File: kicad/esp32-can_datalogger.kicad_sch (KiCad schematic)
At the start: 60 parts, among them J1 USB_C_Receptacle_USB2.0_16P, J2 USB_C_Receptacle_USB2.0_16P, J3 USB_C_Receptacle_USB2.0_16P, J4 USB_C_Receptacle_USB2.0_16P, J5 USB_C_Receptacle_USB2.0_16P, J6 USB_C_Receptacle_USB2.0_16P, J7 Conn_Coaxial, J8 MicroSD, J9 Conn_01x04_Socket, SW1 SW_Push, SW2 SW_Push, SW3 SW_Push, SW4 SW_Push, U2 PA1616D, U3 PI4ULS3V204LEX, U4 AZ1117-1.8, U5 TJA1051T, U6 TJA1051T, U7 ICM-20948

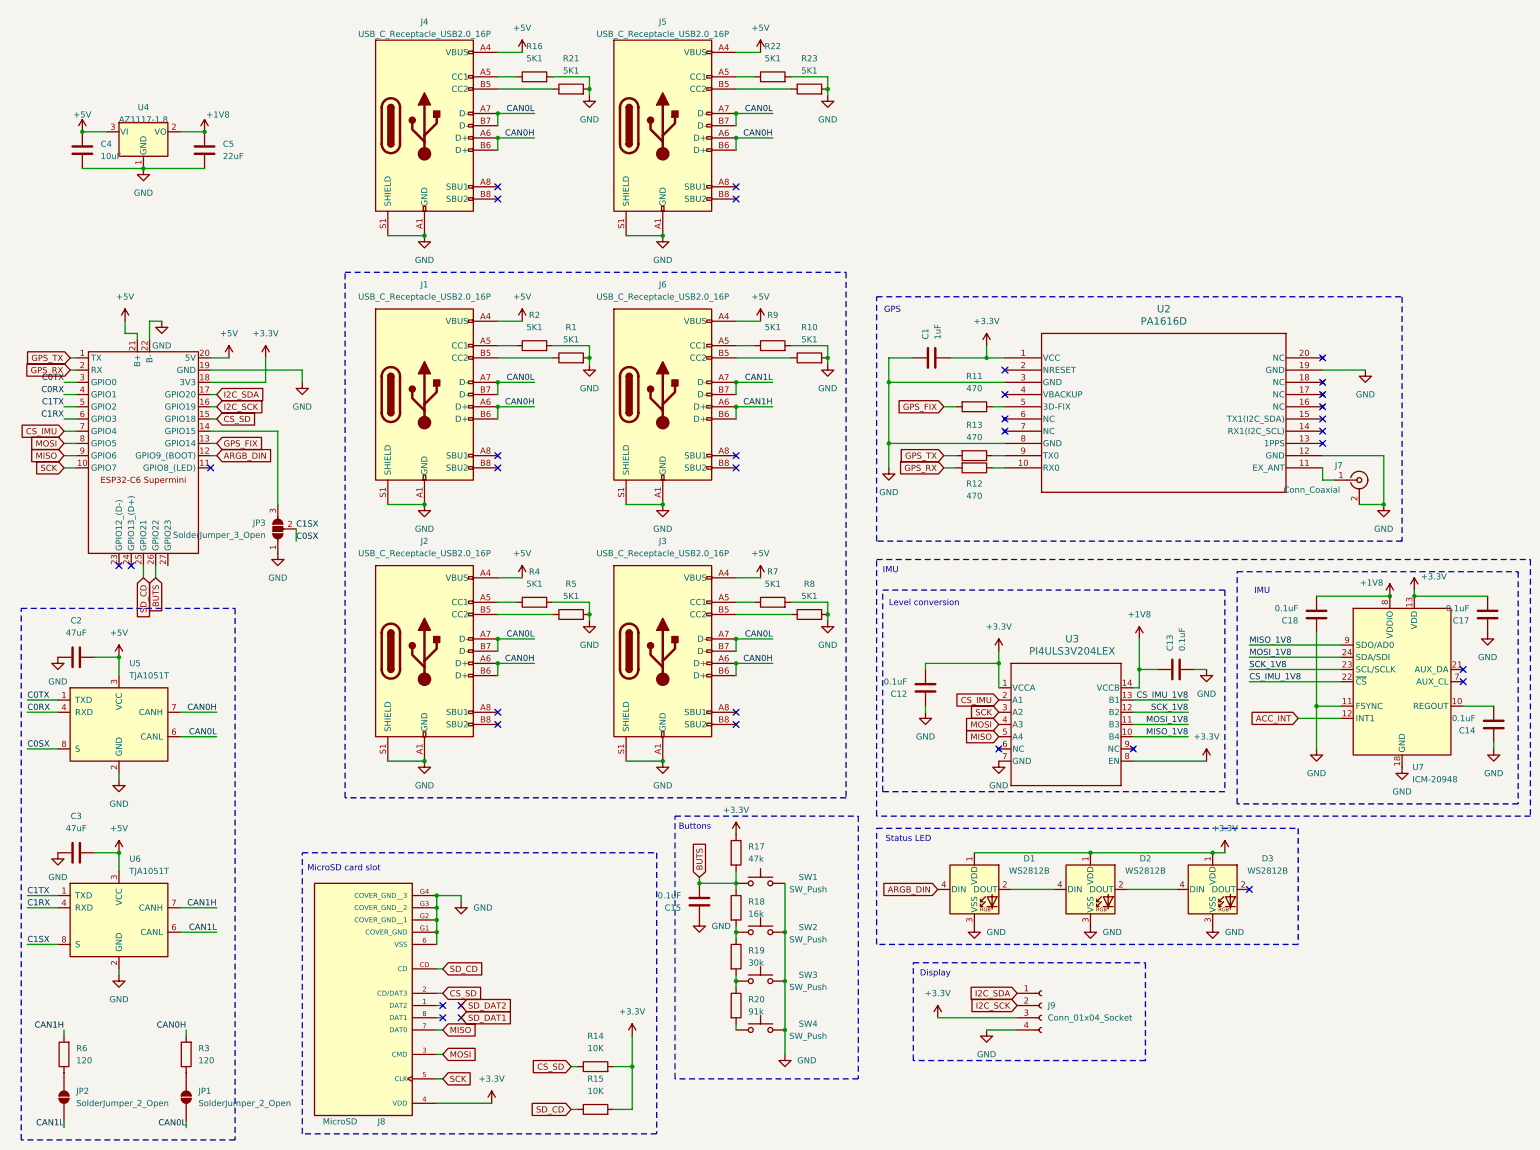
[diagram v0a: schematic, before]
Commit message: switch RX-TX for GPS
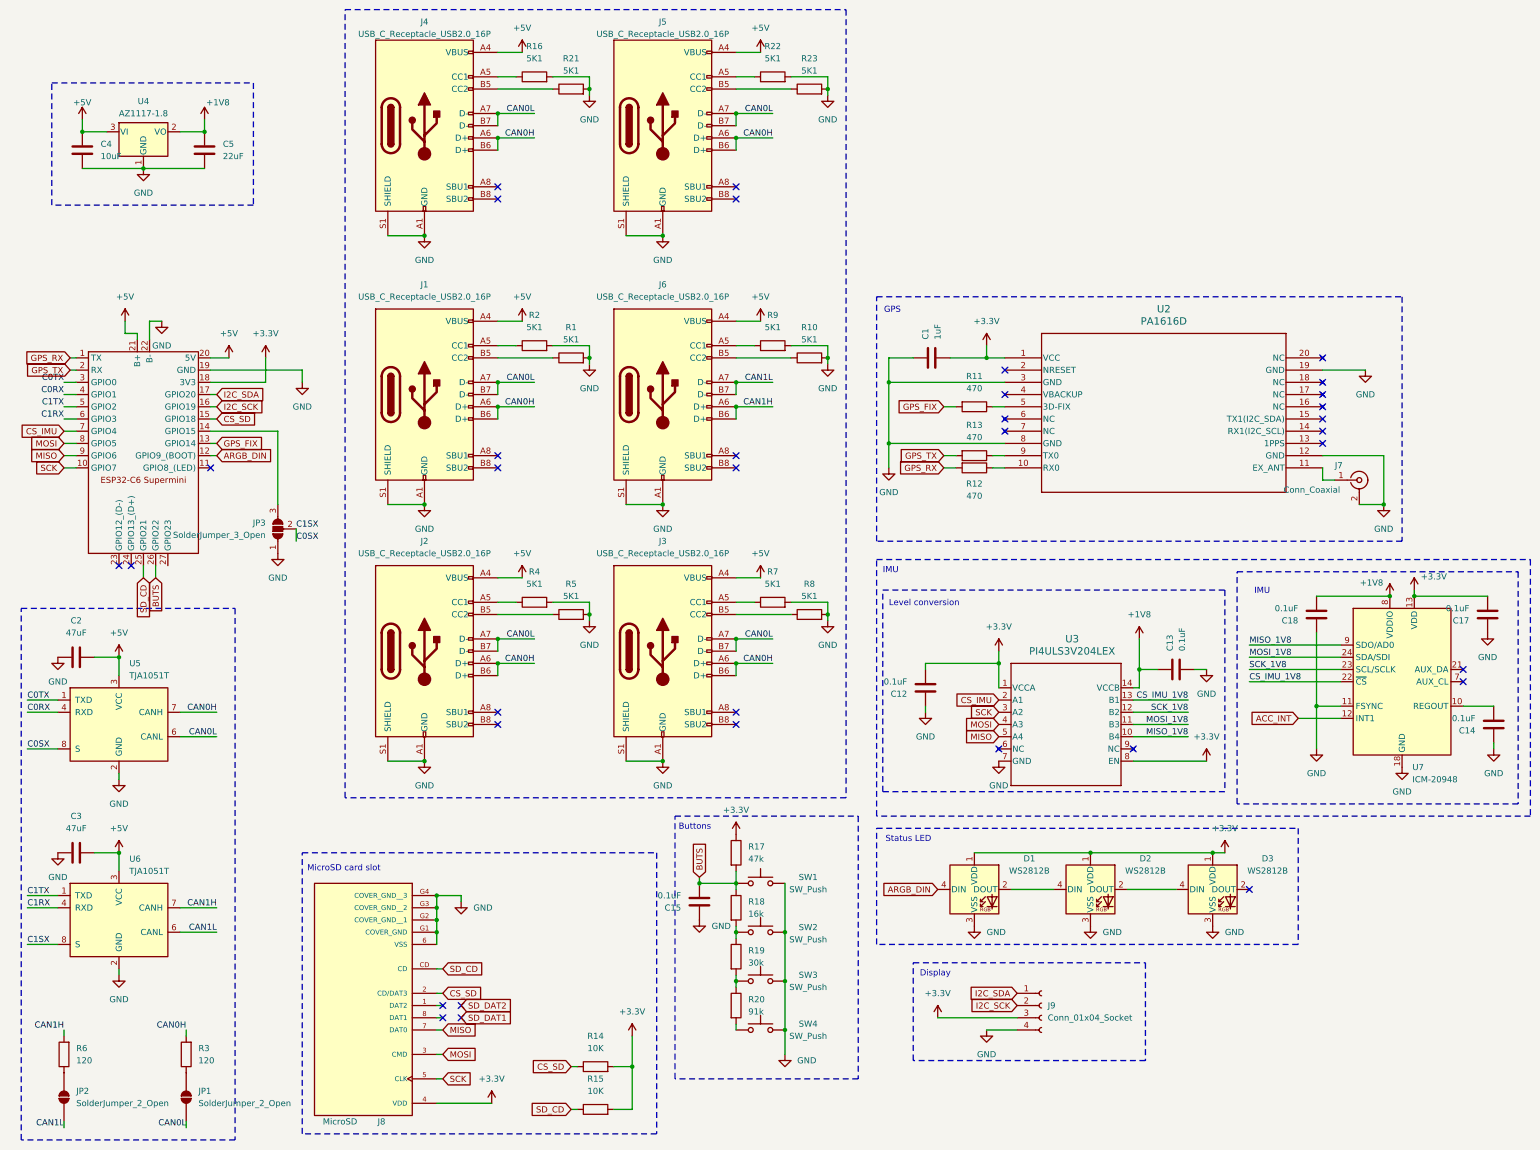
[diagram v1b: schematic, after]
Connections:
- net GPS_RX: now also U1.1 (TX); no longer U1.2 (RX)
- net GPS_TX: now also U1.2 (RX); no longer U1.1 (TX)
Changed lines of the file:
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@@
 	)
 	(rectangle
-		(start 81.28 12.7)
+		(start 20.32 -26.67)
+		(end 62.23 -1.27)
+		(stroke
+			(width 0)
+			(type dash)
+		)
+		(fill
+			(type none)
+		)
+	)
+	(rectangle
+		(start 81.28 -41.91)
 		(end 185.42 121.92)
 		(stroke
@@
 	)
 	(junction
+		(at 26.67 -16.51)
+		(diameter 0)
+		(color 0 0 0 0)
+	)
+	(junction
 		(at 147.32 114.3)
 		(diameter 0)
@@
 	)
 	(junction
-		(at 26.67 -16.51)
-		(diameter 0)
-		(color 0 0 0 0)
-	)
-	(junction
 		(at 97.79 60.96)
 		(diameter 0)
@@
 	(wire
 		(pts
+			(xy 52.07 -19.05) (xy 52.07 -16.51)
+		)
+		(stroke
+			(width 0)
+			(type default)
+		)
+	)
+	(wire
+		(pts
 			(xy 113.03 40.64) (xy 120.65 40.64)
 		)
@@
 	(wire
 		(pts
+			(xy 26.67 -19.05) (xy 26.67 -16.51)
+		)
+		(stroke
+			(width 0)
+			(type default)
+		)
+	)
+	(wire
+		(pts
 			(xy 34.29 92.71) (xy 34.29 96.52)
 		)
@@
 		)
 	)
+	(global_label "GPS_TX"
+		(shape input)
+		(at 24.13 33.02 180)
+		(fields_autoplaced yes)
+		(effects
+			(font
+				(size 1.27 1.27)
+			)
+			(justify right)
+		)
+		(property "Intersheetrefs" "${INTERSHEET_REFS}"
+			(at 14.2506 33.02 0)
+			(hide yes)
+			(show_name no)
+			(do_not_autoplace no)
+			(effects
+				(font
+					(size 1.27 1.27)
+				)
+				(justify right)
+			)
+		)
+	)
 	(global_label "CS_SD"
 		(shape input)
@@
 		)
 	)
+	(global_label "GPS_RX"
+		(shape input)
+		(at 24.13 30.48 180)
+		(fields_autoplaced yes)
+		(effects
+			(font
+				(size 1.27 1.27)
+			)
+			(justify right)
+		)
+		(property "Intersheetrefs" "${INTERSHEET_REFS}"
+			(at 13.9482 30.48 0)
+			(hide yes)
+			(show_name no)
+			(do_not_autoplace no)
+			(effects
+				(font
+					(size 1.27 1.27)
+				)
+				(justify right)
+			)
+		)
+	)
 	(global_label "SCK"
 		(shape input)
@@
 		)
 	)
-	(global_label "GPS_RX"
-		(shape input)
-		(at 24.13 33.02 180)
-		(fields_autoplaced yes)
-		(effects
-			(font
-				(size 1.27 1.27)
-			)
-			(justify right)
-		)
-		(property "Intersheetrefs" "${INTERSHEET_REFS}"
-			(at 13.9482 33.02 0)
-			(hide yes)
-			(show_name no)
-			(do_not_autoplace no)
-			(effects
-				(font
-					(size 1.27 1.27)
-				)
-				(justify right)
-			)
-		)
-	)
 	(global_label "SCK"
 		(shape input)
@@
 		)
 	)
-	(global_label "GPS_TX"
-		(shape input)
-		(at 24.13 30.48 180)
-		(fields_autoplaced yes)
-		(effects
-			(font
-				(size 1.27 1.27)
-			)
-			(justify right)
-		)
-		(property "Intersheetrefs" "${INTERSHEET_REFS}"
-			(at 14.2506 30.48 0)
-			(hide yes)
-			(show_name no)
-			(do_not_autoplace no)
-			(effects
-				(font
-					(size 1.27 1.27)
-				)
-				(justify right)
-			)
-		)
-	)
 	(global_label "I2C_SDA"
 		(shape input)
@@
 	(symbol
 		(lib_id "power:+5V")
-		(at 26.67 -16.51 0)
+		(at 26.67 -19.05 0)
 		(unit 1)
 		(body_style 1)
@@
 		(dnp no)
 		(property "Reference" "#PWR059"
-			(at 26.67 -12.7 0)
+			(at 26.67 -15.24 0)
 			(hide yes)
 			(show_name no)
@@
 		)
 		(property "Value" "+5V"
-			(at 26.67 -20.066 0)
+			(at 26.67 -22.606 0)
 			(show_name no)
 			(do_not_autoplace no)
@@
 		)
 		(property "Footprint" ""
-			(at 26.67 -16.51 0)
+			(at 26.67 -19.05 0)
 			(hide yes)
 			(show_name no)
@@
 		)
 		(property "Datasheet" ""
-			(at 26.67 -16.51 0)
+			(at 26.67 -19.05 0)
 			(hide yes)
 			(show_name no)
@@
 		)
 		(property "Description" "Power symbol creates a global label with name \"+5V\""
-			(at 26.67 -16.51 0)
+			(at 26.67 -19.05 0)
 			(hide yes)
 			(show_name no)
@@
 	(symbol
 		(lib_id "power:+3.3V")
-		(at 52.07 -16.51 0)
+		(at 52.07 -19.05 0)
 		(unit 1)
 		(body_style 1)
@@
 		(dnp no)
 		(property "Reference" "#PWR058"
-			(at 52.07 -12.7 0)
+			(at 52.07 -15.24 0)
 			(hide yes)
 			(show_name no)
@@
 		)
 		(property "Value" "+1V8"
-			(at 54.864 -20.066 0)
+			(at 54.864 -22.606 0)
 			(show_name no)
 			(do_not_autoplace no)
@@
 		)
 		(property "Footprint" ""
-			(at 52.07 -16.51 0)
+			(at 52.07 -19.05 0)
 			(hide yes)
 			(show_name no)
@@
 		)
 		(property "Datasheet" ""
-			(at 52.07 -16.51 0)
+			(at 52.07 -19.05 0)
 			(hide yes)
 			(show_name no)
@@
 		)
 		(property "Description" "Power symbol creates a global label with name \"+3.3V\""
-			(at 52.07 -16.51 0)
+			(at 52.07 -19.05 0)
 			(hide yes)
 			(show_name no)
@@
 		(in_pos_files yes)
 		(dnp no)
-		(fields_autoplaced yes)
 		(property "Reference" "U4"
-			(at 39.37 -21.59 0)
+			(at 39.37 -22.86 0)
 			(show_name no)
 			(do_not_autoplace no)
@@
 		)
 		(property "Value" "AZ1117-1.8"
-			(at 39.37 -19.05 0)
+			(at 39.37 -20.32 0)
 			(show_name no)
 			(do_not_autoplace no)
